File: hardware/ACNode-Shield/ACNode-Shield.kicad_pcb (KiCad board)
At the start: 2 copper layers, 50 x 50 mm, 16 parts, among them J1 MICRO_SD_HINGE, P1 CONN_NFC, P2 CONN_RELAY, P3 CONN_RGB_LED, P4 CONN_X6, P5 CONN_X7, P6 CONN_WS2812, Q1 PN2222A, SW1 SW_RST, SW2 SW_BTN, U1 SRD-05VDC-SL-C, U2 WS2812B

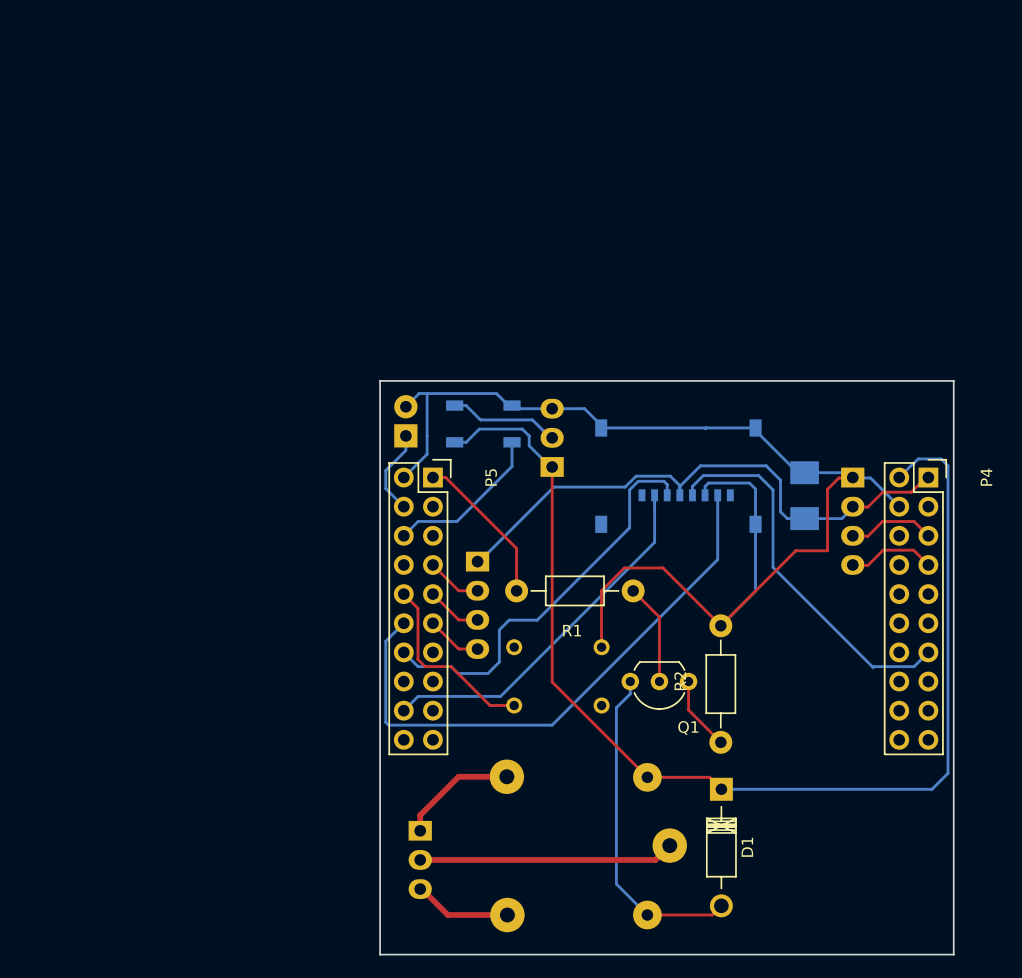
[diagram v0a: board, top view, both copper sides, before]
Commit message: Simplified PCB, changed Micro SD slot footprint.
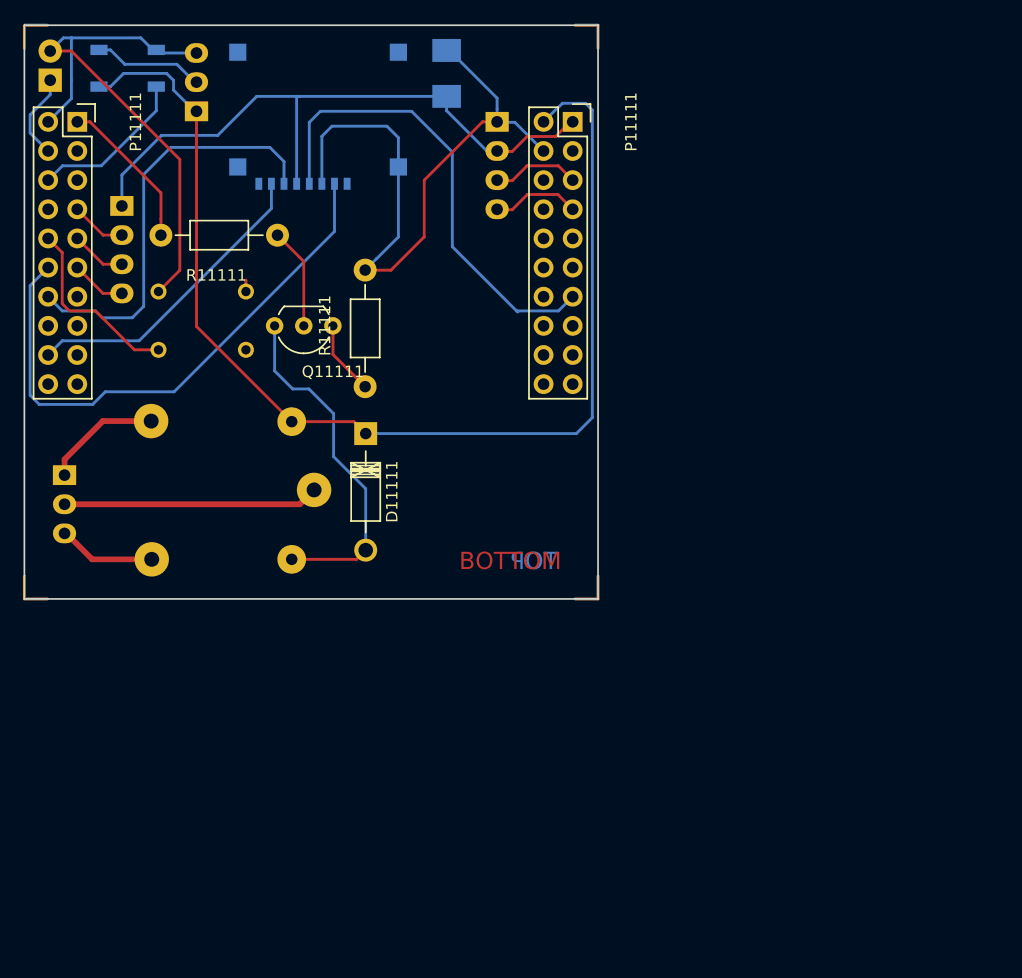
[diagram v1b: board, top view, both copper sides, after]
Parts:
- moved C11111 48.2 mm to (55.8, 23.2)
- moved D11111 43.8 mm to (48.7, 54.6)
- moved P11111 43.8 mm to (60.2, 27.4)
- moved P11111 43.8 mm to (27.5, 34.8)
- moved P11111 43.8 mm to (66.8, 27.4)
- moved P11111 43.8 mm to (23.6, 27.4)
- moved P11111 43.8 mm to (34.0, 26.5)
- moved Q11111 43.8 mm to (45.9, 45.2)
- moved R11111 43.8 mm to (41.1, 37.3)
- moved R11111 43.8 mm to (48.7, 50.5)
- moved SW11111 43.8 mm to (34.5, 44.8)
- moved SW11111 43.8 mm to (21.2, 23.8)
- moved U11111 43.8 mm to (44.2, 59.5)
- moved U11111 43.8 mm to (28.0, 22.8)
- moved P11111 43.8 mm to (22.5, 58.2)
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- renumbered C1 to C11111, D1 to D11111, J1 to J11111, P1 to P11111, P2 to P11111, P3 to P11111, P4 to P11111, P5 to P11111, P6 to P11111, Q1 to Q11111, R1 to R11111, R2 to R11111, SW1 to SW11111, SW2 to SW11111, U1 to U11111, U2 to U11111
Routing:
- net (no net): track 0.00 -> 32.0 mm
- net PQ0: track 33.2 -> 41.4 mm
- net +3.3v: track 50.1 -> 56.4 mm
- net PQ1: track 32.0 -> 26.9 mm
- net GND: track 113.0 -> 108.4 mm
- net Net-(D1-Pad2): track 28.8 -> 30.4 mm
- net PQ3: track 35.3 -> 36.7 mm
- net PQ2: track 49.9 -> 49.0 mm
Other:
- board text added: "BOTTOM"
- board text added: "TOP"

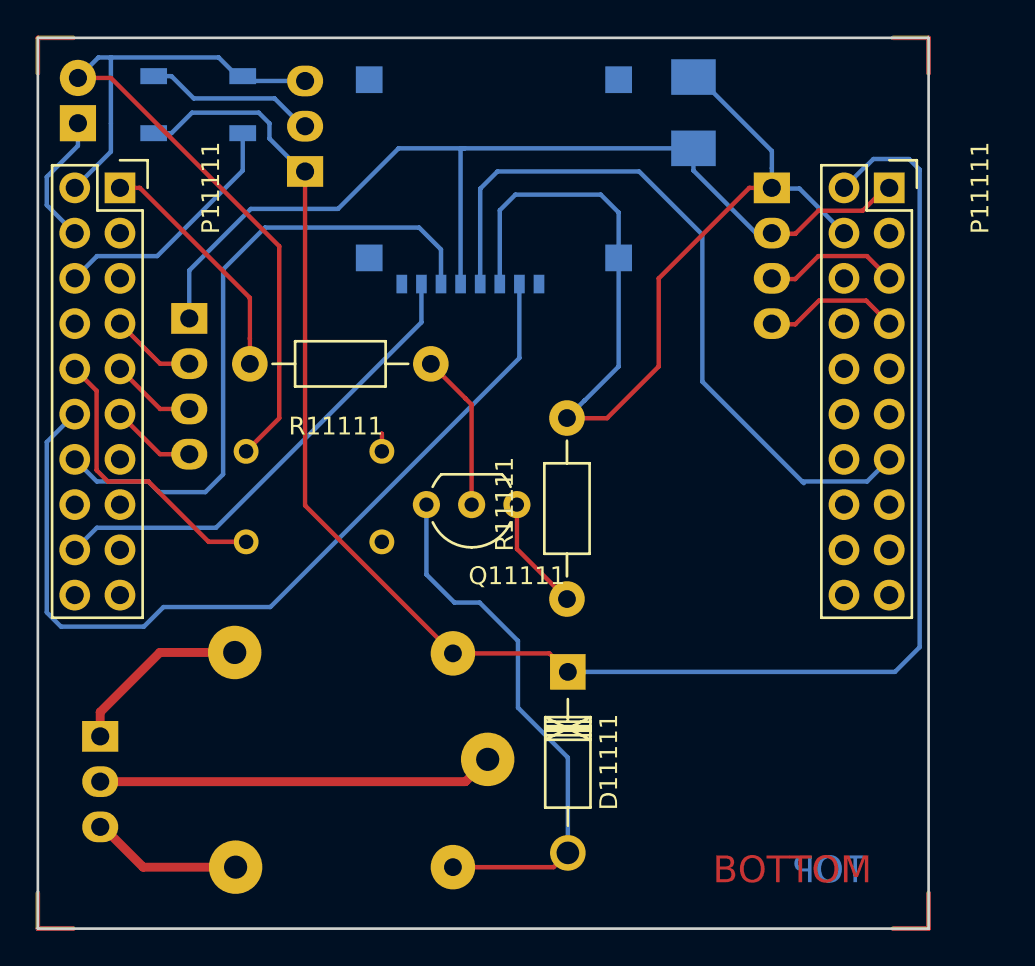
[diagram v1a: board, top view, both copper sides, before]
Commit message: Removed a resistor, fixed some tracks.
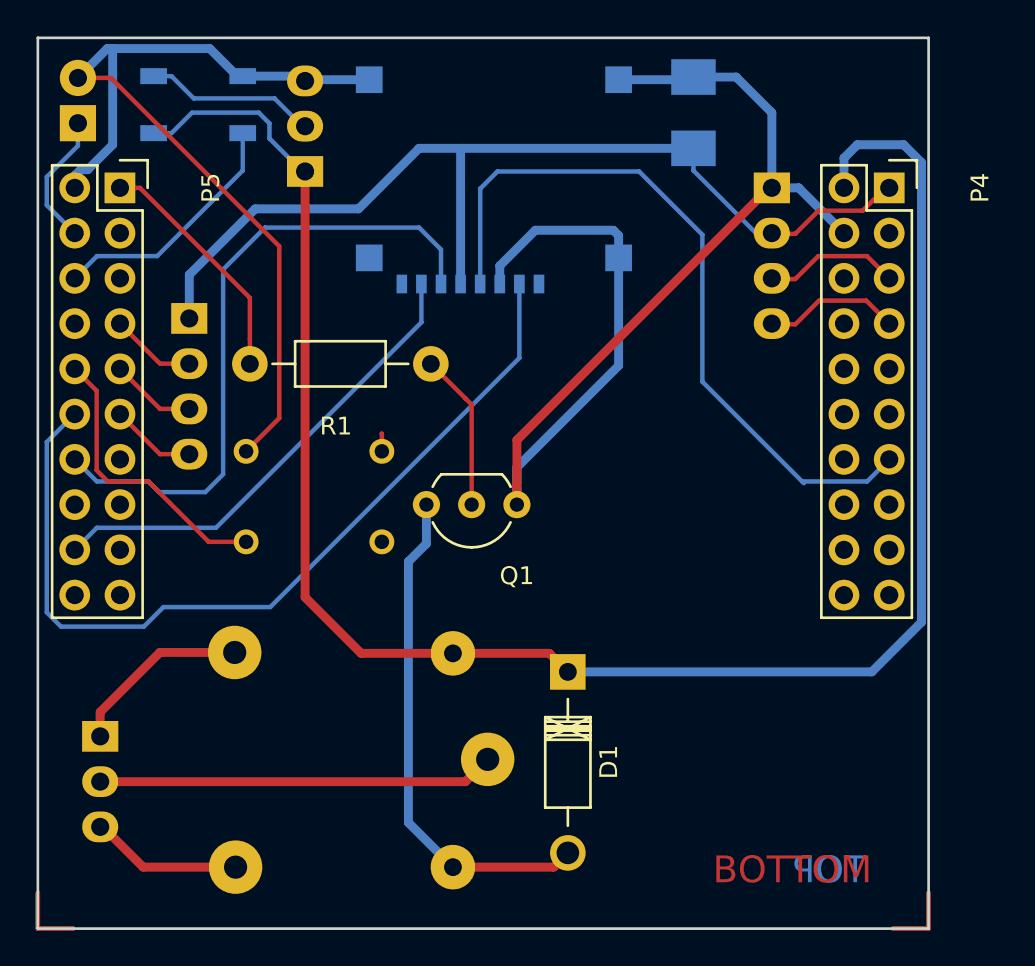
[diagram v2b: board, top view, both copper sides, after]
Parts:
- removed R11111: 100, Resistors_ThroughHole:Resistor_Horizontal_RM10mm
- R1: renamed from R11111; value 10k -> 1k
- renumbered C11111 to C1, D11111 to D1, J11111 to J1, P11111 to P1, P11111 to P2, P11111 to P3, P11111 to P4, P11111 to P5, P11111 to P6, Q11111 to Q1, SW11111 to SW1, SW11111 to SW2, U11111 to U1, U11111 to U2
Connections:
- Q1 pad 1: Net-(Q1-Pad1) -> GND
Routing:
- net GND: track 108.4 -> 125.4 mm
- net (no net): track 32.0 -> 16.0 mm
- net Net-(Q1-Pad1): track 6.46 -> 0.00 mm
- net +5V: track 100.5 -> 104.8 mm
- net Net-(D1-Pad2): track 30.4 -> 28.6 mm
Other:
- net class +3.3v added: clearance 0.2, trace_width 0.5, via_dia 0.6, via_drill 0.4
- net class +5V added: clearance 0.2, trace_width 0.5, via_dia 0.6, via_drill 0.4
- net class GND added: clearance 0.2, trace_width 0.5, via_dia 0.6, via_drill 0.4

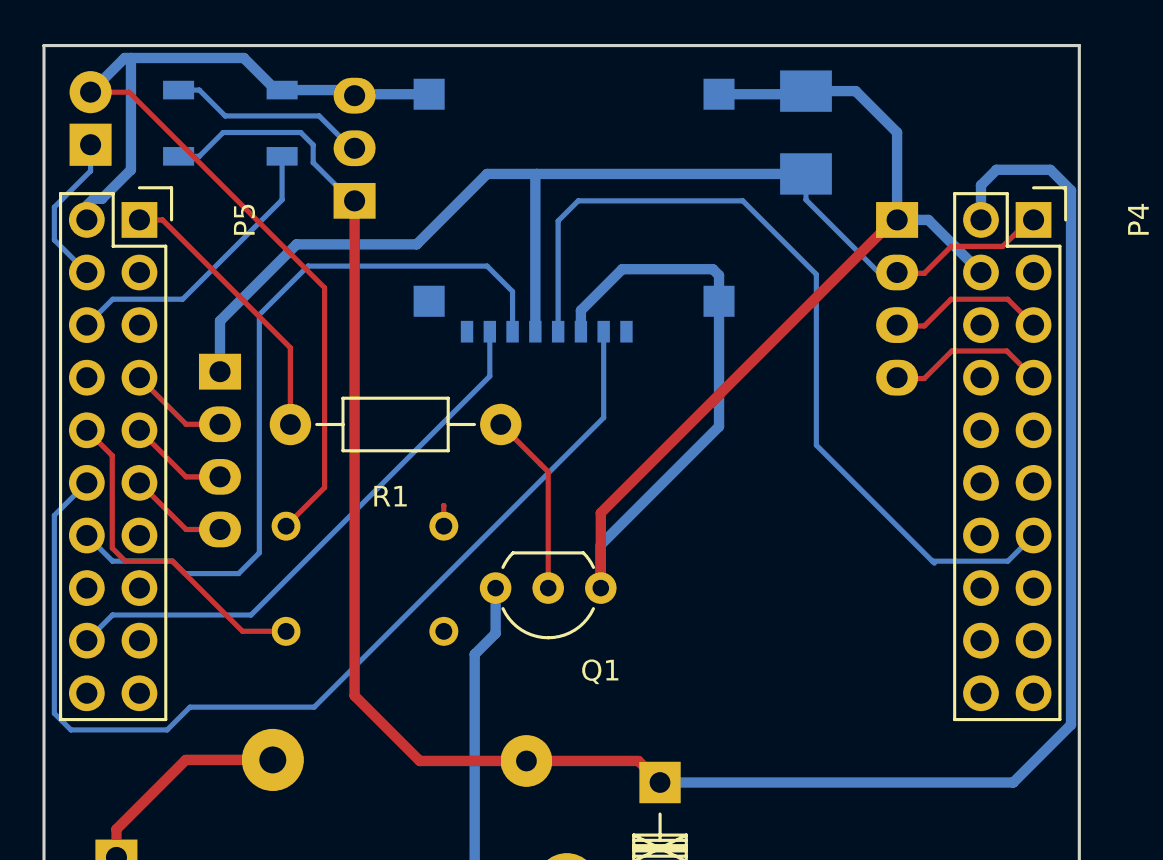
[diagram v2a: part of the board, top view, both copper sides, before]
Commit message: Moved components around, changed MicroSD card receptacle footprint (was flipped (!)).
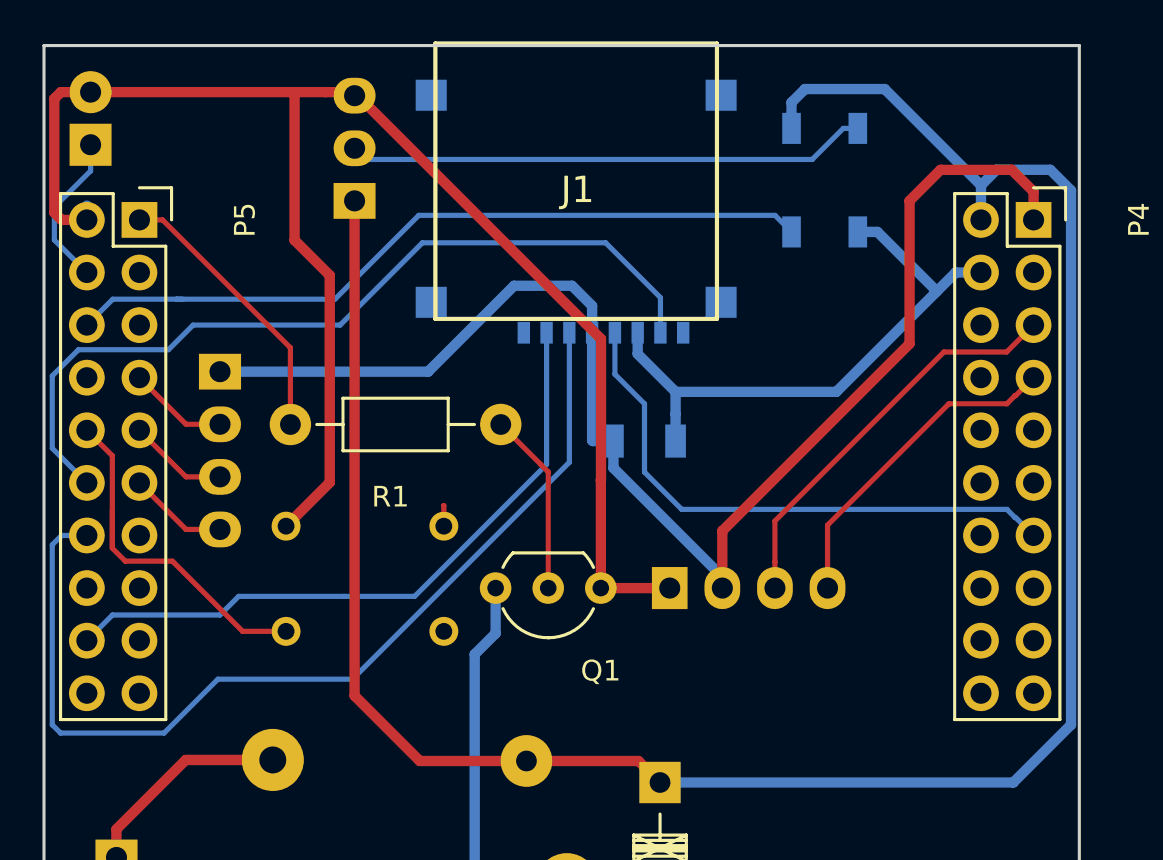
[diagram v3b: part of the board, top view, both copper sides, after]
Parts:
- C1: value 10nF -> C_Small; footprint Capacitors_SMD:C_1210_HandSoldering -> Capacitors_SMD:C_1206
- J1: footprint armory:MICRO_SD_HINGE_AMP -> MicroSD:MICRO_SD_HINGE_CHINA; moved to F.Cu
- moved U2 28.8 mm to (56.7, 25.5), turned to 180 degrees
- moved P1 20.9 mm to (49.2, 45.2), turned to 270 degrees
- moved C1 16.8 mm to (48.0, 38.1), turned to 0 degrees
- moved J1 4.10 mm to (46.7, 23.4), turned to 0 degrees
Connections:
- C1 pad 1: GND -> +3.3v
- C1 pad 2: +3.3v -> GND
- J1 pad 10: GND -> (no net)
- J1 pad 11: GND -> (no net)
- J1 pad 12: GND -> (no net)
- J1 pad 9: GND -> (no net)
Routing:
- net PP5: track 14.0 -> 36.9 mm
- net GND: track 125.4 -> 109.1 mm
- net Net-(P6-Pad2): track 9.66 -> 25.3 mm
- net PQ0: track 41.4 -> 27.4 mm
- net PP0: track 7.59 -> 19.7 mm
- net +3.3v: track 56.1 -> 68.0 mm
- net PQ3: track 36.7 -> 47.4 mm
- net PQ2: track 49.0 -> 40.7 mm
- net PP1: track 7.63 -> 15.9 mm
- net PQ1: track 26.9 -> 32.1 mm
- net +5V: track 104.8 -> 106.7 mm
- net /RESET: track 16.3 -> 18.1 mm
